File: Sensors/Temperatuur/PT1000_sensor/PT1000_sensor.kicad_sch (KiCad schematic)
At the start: 26 parts, among them J1 Conn_01x02_Pin, J2 Conn_01x02_Pin, J3 Conn_01x02_Pin, Q1 BC546, U1 LTC2055

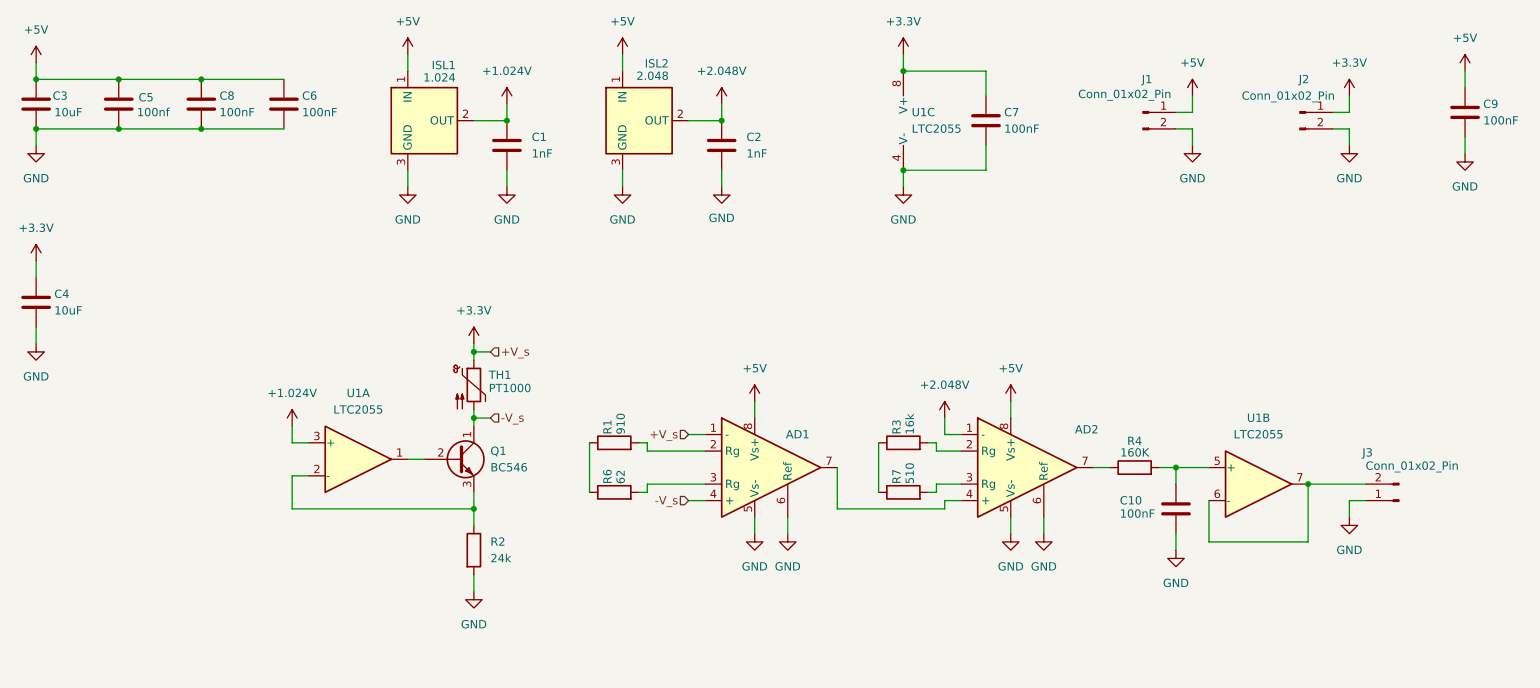
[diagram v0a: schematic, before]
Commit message: made a way to cut the power to the AD8226
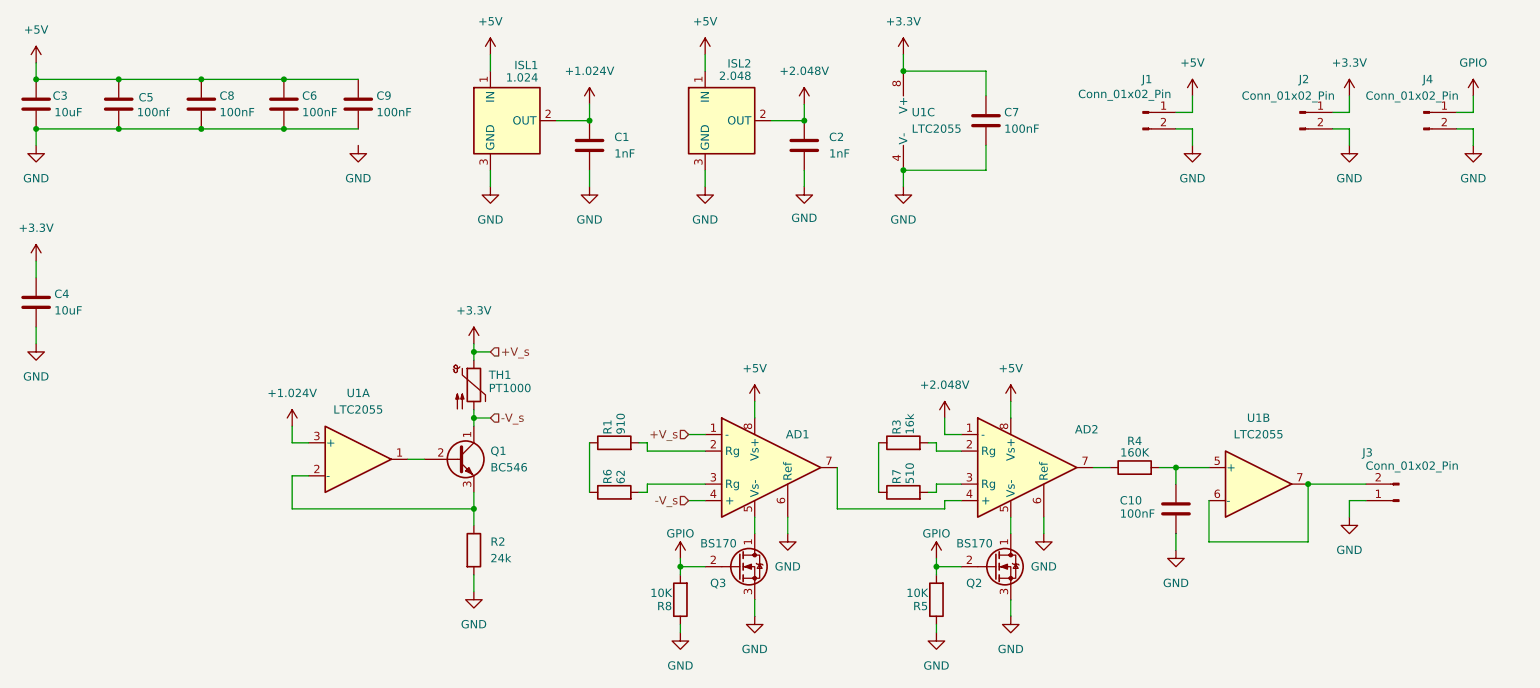
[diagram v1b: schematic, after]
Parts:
- added J4: Conn_01x02_Pin, Connector_PinHeader_1.00mm:PinHeader_1x02_P1.00mm_Vertical, symbol Connector:Conn_01x02_Pin
- added Q2, Q3: BS170, Package_TO_SOT_THT:TO-92_Inline, symbol Transistor_FET:BS170
- added R5, R8: 10K, Resistor_SMD:R_0805_2012Metric, symbol Device:R
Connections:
- net GND: now also J4.2 (Pin_2), Q2.3 (S), Q3.3 (S), R5.1, R8.1; no longer AD1.5 (Vs-), AD2.5 (Vs-)
- new net: AD2.5 (Vs-), Q2.1 (D)
- new net: AD1.5 (Vs-), Q3.1 (D)
- new net GPIO: J4.1 (Pin_1), Q2.2 (G), Q3.2 (G), R5.2, R8.2
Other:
- moved on the sheet: C1, C2, C9, ISL1, ISL2

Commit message: added new features for evaulation
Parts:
- AD1, AD2: value ~ -> AD8226
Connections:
- net +3.3V: now also AD1.4 (+); no longer AD1.1 (-)
- net -V_s: now also AD1.1 (-); no longer AD1.4 (+)
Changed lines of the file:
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@@
+	(wire
+		(pts
+			(xy 86.36 74.93) (xy 86.36 76.2)
+		)
+		(stroke
+			(width 0)
+			(type default)
+		)
+	)
+	(wire
+		(pts
+			(xy 168.91 72.39) (xy 168.91 74.93)
+		)
+		(stroke
+			(width 0)
+			(type default)
+		)
+	)
+	(wire
+		(pts
+			(xy 19.05 60.96) (xy 19.05 63.5)
+		)
+		(stroke
+			(width 0)
+			(type default)
+		)
+	)
 	(wire
 		(pts
@@
 	(wire
 		(pts
-			(xy 86.36 74.93) (xy 86.36 76.2)
-		)
-		(stroke
-			(width 0)
-			(type default)
-		)
-	)
-	(wire
-		(pts
-			(xy 168.91 72.39) (xy 168.91 74.93)
-		)
-		(stroke
-			(width 0)
-			(type default)
-		)
-	)
-	(wire
-		(pts
-			(xy 19.05 60.96) (xy 19.05 63.5)
-		)
-		(stroke
-			(width 0)
-			(type default)
-		)
-	)
-	(wire
-		(pts
 			(xy 157.48 85.09) (xy 161.29 85.09)
 		)
@@
 	(wire
 		(pts
+			(xy 119.38 77.47) (xy 121.92 77.47)
+		)
+		(stroke
+			(width 0)
+			(type default)
+		)
+	)
+	(wire
+		(pts
 			(xy 137.16 26.67) (xy 137.16 29.21)
 		)
@@
 	(wire
 		(pts
-			(xy 119.38 77.47) (xy 121.92 77.47)
-		)
-		(stroke
-			(width 0)
-			(type default)
-		)
-	)
-	(wire
-		(pts
 			(xy 218.44 30.48) (xy 220.98 30.48)
 		)
@@
 			(width 0)
 			(type default)
-		)
-	)
-	(hierarchical_label "-V_s"
-		(shape input)
-		(at 119.38 87.63 180)
-		(fields_autoplaced yes)
-		(effects
-			(font
-				(size 1.27 1.27)
-			)
-			(justify right)
 		)
 	)
@@
 	(hierarchical_label "-V_s"
 		(shape input)
+		(at 119.38 77.47 180)
+		(fields_autoplaced yes)
+		(effects
+			(font
+				(size 1.27 1.27)
+			)
+			(justify right)
+		)
+	)
+	(hierarchical_label "+V_s"
+		(shape input)
+		(at 119.38 87.63 180)
+		(fields_autoplaced yes)
+		(effects
+			(font
+				(size 1.27 1.27)
+			)
+			(justify right)
+		)
+	)
+	(hierarchical_label "-V_s"
+		(shape input)
 		(at 88.9 74.93 0)
 		(fields_autoplaced yes)
@@
 			)
 			(justify left)
-		)
-	)
-	(hierarchical_label "+V_s"
-		(shape input)
-		(at 119.38 77.47 180)
-		(fields_autoplaced yes)
-		(effects
-			(font
-				(size 1.27 1.27)
-			)
-			(justify right)
 		)
 	)
@@
 		(dnp no)
 		(property "Reference" "AD2"
-			(at 180.594 76.708 0)
-			(effects
-				(font
-					(size 1.27 1.27)
-				)
-			)
-		)
-		(property "Value" "~"
-			(at 182.88 79.4065 0)
+			(at 176.53 76.962 0)
+			(effects
+				(font
+					(size 1.27 1.27)
+				)
+			)
+		)
+		(property "Value" "AD8226"
+			(at 175.768 74.93 0)
 			(effects
 				(font
@@
 		(dnp no)
 		(property "Reference" "AD1"
-			(at 136.144 77.47 0)
-			(effects
-				(font
-					(size 1.27 1.27)
-				)
-			)
-		)
-		(property "Value" "~"
-			(at 143.51 79.4065 0)
-			(effects
-				(font
+			(at 135.636 77.47 0)
+			(effects
+				(font
+					(size 1.27 1.27)
+				)
+			)
+		)
+		(property "Value" "AD8226"
+			(at 135.128 75.692 0)
+			(effects
+				(font
